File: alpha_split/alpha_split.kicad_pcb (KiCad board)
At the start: 2 copper layers, 109 x 71 mm, 135 parts, among them J1 USB_OTG, J2 USB_OTG, J3 PDI, J4 D4, J5 D5, J6 A6, J7 A7, J8 B0, J9 E2, K00 K00, K01 K01, K02 K02, K03 K03, K04 K04, K05 K05, K10 K10, K11 K11, K12 K12, K13 K13, K14 K14, K15 K15, K20 K20, K21 K21, K22 K22, K23 K23, K24 K24, K25 K25, K30 K30, K31 K31, K32 K32, K33 K33, K34 K34, K35 K35, SW1 Switch-6P-2S2T, SW2 RST_SW, U1 MCP73831, U2 MCP1700 (3.0V), U3 MCP1700 (3.3V), U4 ATXMEGA-A4U-EPAD, U5 74LVC1G34, U6 nRF24L01_module, U7 FSUSB42, U8 FSUSB42, U9 FSUSB42

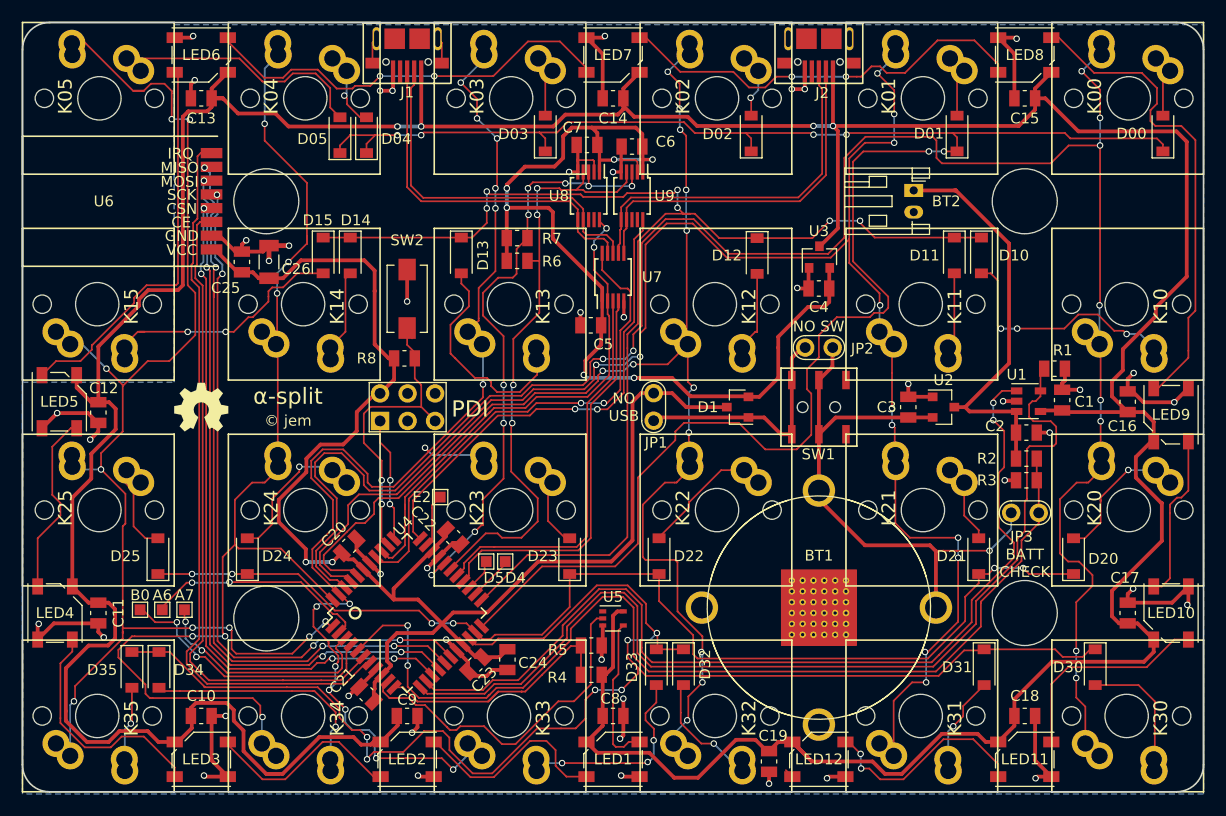
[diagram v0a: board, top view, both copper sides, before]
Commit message: minor PCB fixes and BOM updates
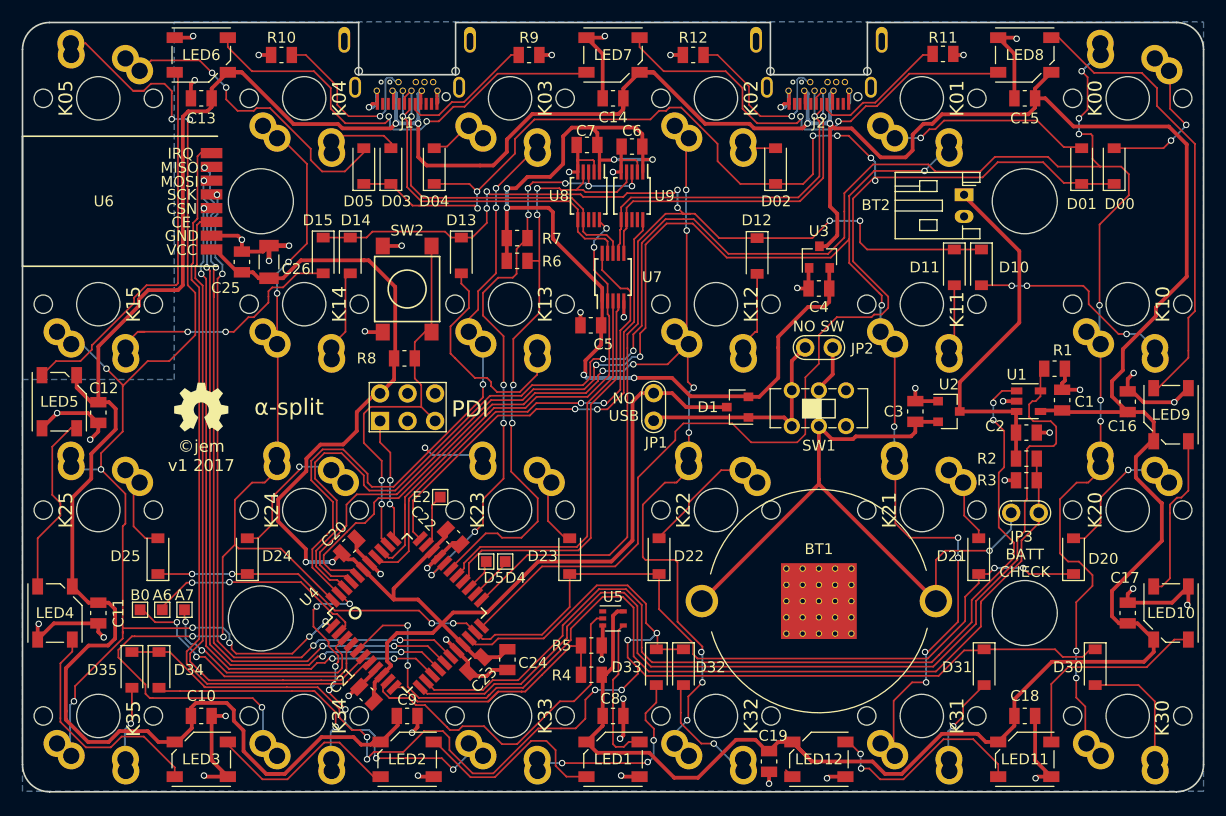
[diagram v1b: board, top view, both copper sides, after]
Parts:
- removed the BT1 at (73.5, 54.0) (x2)
- removed the REF** at (73.5, 56.0)
- removed the REF** at (75.5, 56.0)
- removed the REF** at (75.5, 54.0)
- removed the REF** at (75.5, 52.0)
- removed the REF** at (71.5, 54.0)
- removed the REF** at (73.5, 52.0)
- removed the REF** at (73.5, 54.0)
- removed the REF** at (71.5, 52.0)
- added BT1: Battery, battery:CR2032_BK-913, F.Cu at (73.5, 53.4)
- added R10: 5.1k, Resistor_SMD:R_0805_2012Metric, F.Cu at (23.9, 3.00)
- added R11: 5.1k, Resistor_SMD:R_0805_2012Metric, F.Cu at (85.0, 2.90)
- added R12: 5.1k, Resistor_SMD:R_0805_2012Metric, F.Cu at (61.9, 3.00)
- added R9: 5.1k, Resistor_SMD:R_0805_2012Metric, F.Cu at (46.8, 3.00)
- added REF**: StitchVia_0.3mm, StitchVia_2x2_0.3mm, F.Cu at (76.5, 56.4)
- added REF**: StitchVia_0.3mm, StitchVia_2x2_0.3mm, F.Cu at (70.5, 54.9)
- added REF**: StitchVia_0.3mm, StitchVia_2x2_0.3mm, F.Cu at (76.5, 53.4)
- added REF**: StitchVia_0.3mm, StitchVia_2x2_0.3mm, F.Cu at (75.0, 53.4)
- added REF**: StitchVia_0.3mm, StitchVia_2x2_0.3mm, F.Cu at (73.5, 53.4)
- added REF**: StitchVia_0.3mm, StitchVia_2x2_0.3mm, F.Cu at (72.0, 53.4)
- added REF**: StitchVia_0.3mm, StitchVia_2x2_0.3mm, F.Cu at (70.5, 53.4)
- added REF**: StitchVia_0.3mm, StitchVia_2x2_0.3mm, F.Cu at (76.5, 51.9)
- added REF**: StitchVia_0.3mm, StitchVia_2x2_0.3mm, F.Cu at (75.0, 51.9)
- added REF**: StitchVia_0.3mm, StitchVia_2x2_0.3mm, F.Cu at (73.5, 51.9)
- added REF**: StitchVia_0.3mm, StitchVia_2x2_0.3mm, F.Cu at (72.0, 51.9)
- added REF**: StitchVia_0.3mm, StitchVia_2x2_0.3mm, F.Cu at (75.0, 56.4)
- added REF**: StitchVia_0.3mm, StitchVia_2x2_0.3mm, F.Cu at (70.5, 51.9)
- added REF**: StitchVia_0.3mm, StitchVia_2x2_0.3mm, F.Cu at (76.5, 50.4)
- added REF**: StitchVia_0.3mm, StitchVia_2x2_0.3mm, F.Cu at (75.0, 50.4)
- added REF**: StitchVia_0.3mm, StitchVia_2x2_0.3mm, F.Cu at (73.5, 50.4)
- added REF**: StitchVia_0.3mm, StitchVia_2x2_0.3mm, F.Cu at (72.0, 50.4)
- added REF**: StitchVia_0.3mm, StitchVia_2x2_0.3mm, F.Cu at (73.5, 56.4)
- added REF**: StitchVia_0.3mm, StitchVia_2x2_0.3mm, F.Cu at (72.0, 56.4)
- added REF**: StitchVia_0.3mm, StitchVia_2x2_0.3mm, F.Cu at (70.5, 56.4)
- added REF**: StitchVia_0.3mm, StitchVia_2x2_0.3mm, F.Cu at (76.5, 54.9)
- added REF**: StitchVia_0.3mm, StitchVia_2x2_0.3mm, F.Cu at (75.0, 54.9)
- added REF**: StitchVia_0.3mm, StitchVia_2x2_0.3mm, F.Cu at (73.5, 54.9)
- added REF**: StitchVia_0.3mm, StitchVia_2x2_0.3mm, F.Cu at (72.0, 54.9)
- J1, J2: value USB_OTG -> USB_C_Receptacle; footprint conn_usb:USB_Micro -> conn_usb:USB_TypeC_DX07B024XJ1
- K00, K01, K02, K03, K04, K05, K10, K11, K12, K13, K14, K15, K20, K21, K22, K23, K24, K25, K30, K31, K32, K33, K34, K35: footprint switch_mx:Cherry_MX_Matias -> switch_mx:Cherry_MX_Matias_NoSilk_Back
- REF**: footprint kicad_util:StitchVia_2x2_0.3mm -> StitchVia_2x2_0.3mm
- SW1: footprint switch:Switch_Slide_SMD_6 -> switch:SlideSwitch_C&K_JS202011CQN
- SW2: footprint Button_Switch_SMD:SW_SPST_EVQPE1 -> switch:SwitchPush_C&K_PTS645_SMT
- moved D01 11.9 mm to (97.8, 13.2)
- moved D03 10.7 mm to (38.0, 13.2)
- moved REF** 5.69 mm to (70.5, 50.4)
- moved D00 5.41 mm to (100.8, 13.2)
- moved BT2 4.67 mm to (86.9, 15.9)
- moved D02 3.75 mm to (69.5, 13.2)
- moved D04 3.63 mm to (34.0, 13.2)
- moved D05 3.60 mm to (31.5, 13.2)
- moved J1 3.35 mm to (35.5, 6.85)
- moved J2 3.35 mm to (73.5, 6.85)
- moved D10 1.10 mm to (88.5, 22.6)
- moved D11 1.10 mm to (86.0, 22.6)
- moved SW2 0.90 mm to (35.5, 24.6)
- moved C3 0.76 mm to (82.4, 35.9)
- moved U2 0.64 mm to (85.5, 35.9)
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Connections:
- K02 pad 1: Net-(D02-Pad2) -> /COL2
- K02 pad 2: /COL2 -> Net-(D02-Pad2)
- K04 pad 1: Net-(D04-Pad2) -> /COL4
- K04 pad 2: /COL4 -> Net-(D04-Pad2)
- SW2 pad 1: /RST -> GND
- U7 pad 6: /D-_R -> /USB_R_D-
- U7 pad 7: /D+_R -> /USB_R_D+
- U7 pad 8: /D-_L -> /USB_L_D-
- U7 pad 9: /D+_L -> /USB_L_D+
- U8 pad 6: /D+_L -> /USB_L_D+
- U8 pad 7: /D-_L -> /USB_L_D-
- U9 pad 6: /D+_R -> /USB_R_D+
- U9 pad 7: /D-_R -> /USB_R_D-
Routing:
- net /D-_L: track 33.9 -> 0.00 mm
- net /D+_R: track 33.8 -> 0.00 mm
- net /D-_R: track 33.5 -> 0.00 mm
- net /D+_L: track 33.5 -> 0.00 mm
- net /USB_R_D+: track 0.00 -> 33.5 mm, vias 0 -> 1
- net /USB_L_D-: track 0.00 -> 33.4 mm, vias 0 -> 1
- net /USB_L_D+: track 0.00 -> 33.4 mm, vias 0 -> 1
- net /USB_R_D-: track 0.00 -> 33.1 mm, vias 0 -> 1
- net +5V: track 398.9 -> 419.1 mm
- net /BATT_IN: track 54.8 -> 72.6 mm
- net Net-(J2-PadB5): track 0.00 -> 16.5 mm, vias 0 -> 1
- net Net-(J1-PadB5): track 0.00 -> 16.5 mm, vias 0 -> 1
- net Net-(J2-PadA5): track 0.00 -> 12.6 mm
- net Net-(J1-PadA5): track 0.00 -> 12.6 mm
- net Net-(D01-Pad2): track 8.16 -> 20.6 mm, vias 0 -> 1
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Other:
- outline, holes or cut-outs redrawn
- net class Escape added: clearance 0.15, trace_width 0.15, via_dia 0.6, via_drill 0.4
- rule trace_min: 0.1524 -> 0.15
- board text added: "©jem v1 2017"
- board text removed: "© jem"

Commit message: use slots in mx footprint to appease PCB fab
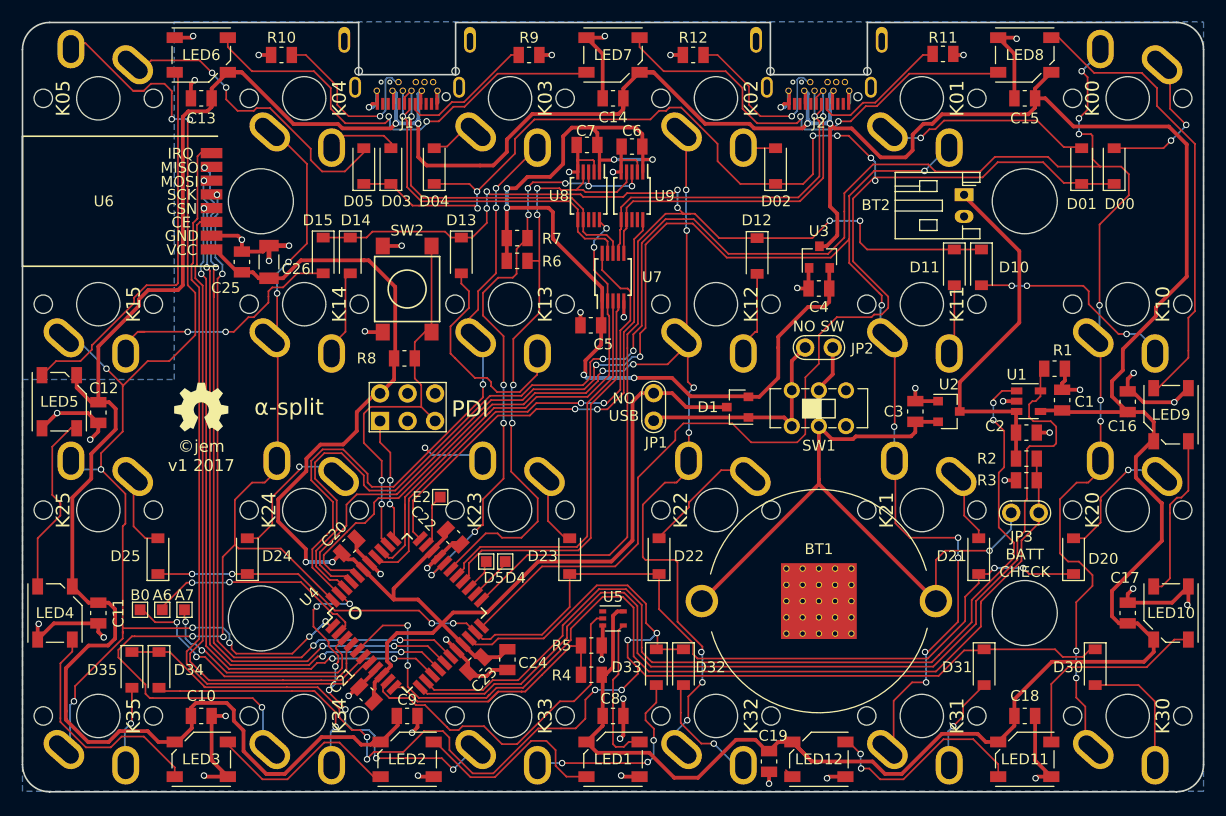
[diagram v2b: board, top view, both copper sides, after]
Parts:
- K00, K01, K02, K03, K04, K05, K10, K11, K12, K13, K14, K15, K20, K21, K22, K23, K24, K25, K30, K31, K32, K33, K34, K35: footprint switch_mx:Cherry_MX_Matias_NoSilk_Back -> switch_mx:Cherry_MX_Matias_Slots_NoSilk_Back
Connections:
- J1 pad S1: (no net) -> Net-(J1-PadS1)
- J2 pad S1: (no net) -> Net-(J2-PadS1)

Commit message: one mounting hole not aligned properly
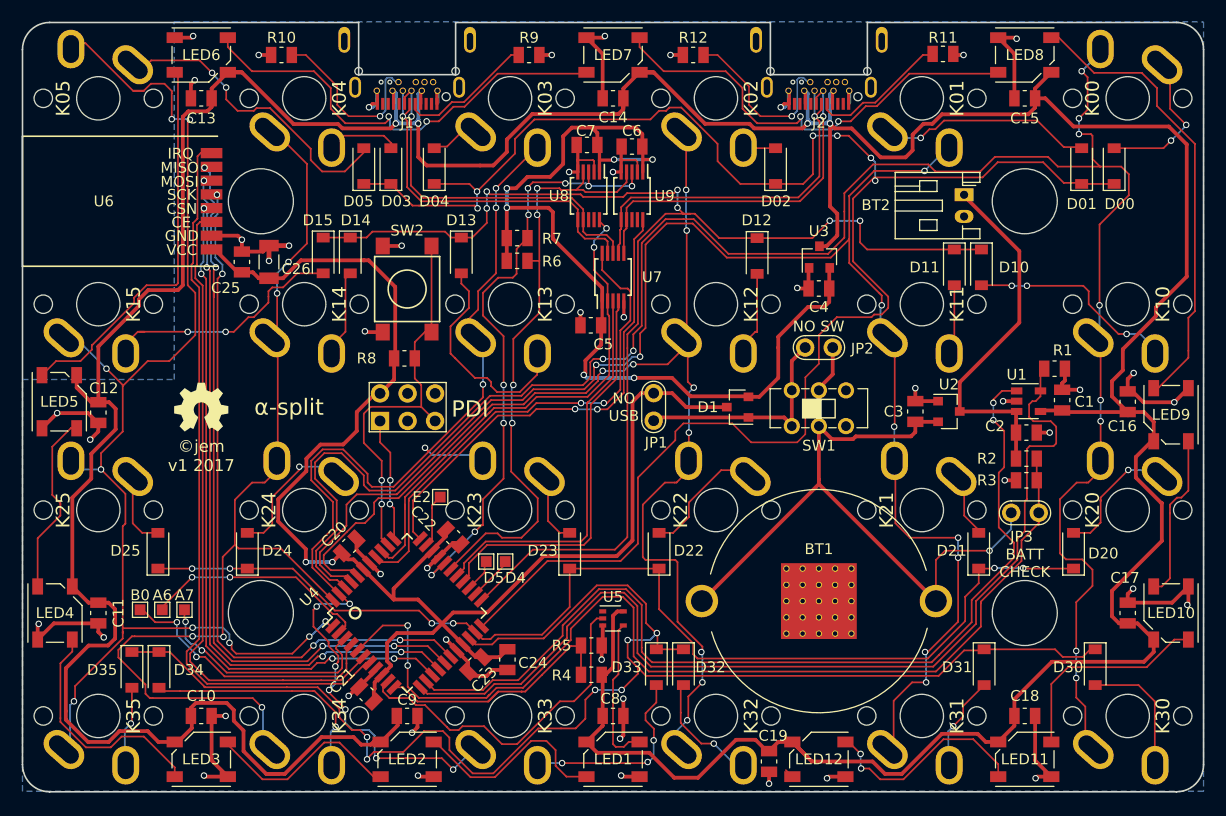
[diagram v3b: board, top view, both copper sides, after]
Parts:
- moved ? 0.50 mm to (22.0, 54.5)
- moved D20 0.50 mm to (97.0, 48.8)
- moved D21 0.50 mm to (88.2, 48.8)
- moved D22 0.50 mm to (58.8, 48.8)
- moved D23 0.50 mm to (50.5, 48.8)
- moved D24 0.50 mm to (20.8, 48.8)
- moved D25 0.50 mm to (12.5, 48.8)
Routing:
- net /ROW2: track 102.5 -> 103.8 mm
- net Net-(D25-Pad2): track 6.96 -> 8.02 mm
- net /A6: track 21.2 -> 21.8 mm
- net Net-(D21-Pad2): track 7.48 -> 6.98 mm

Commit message: reposition mounting holes
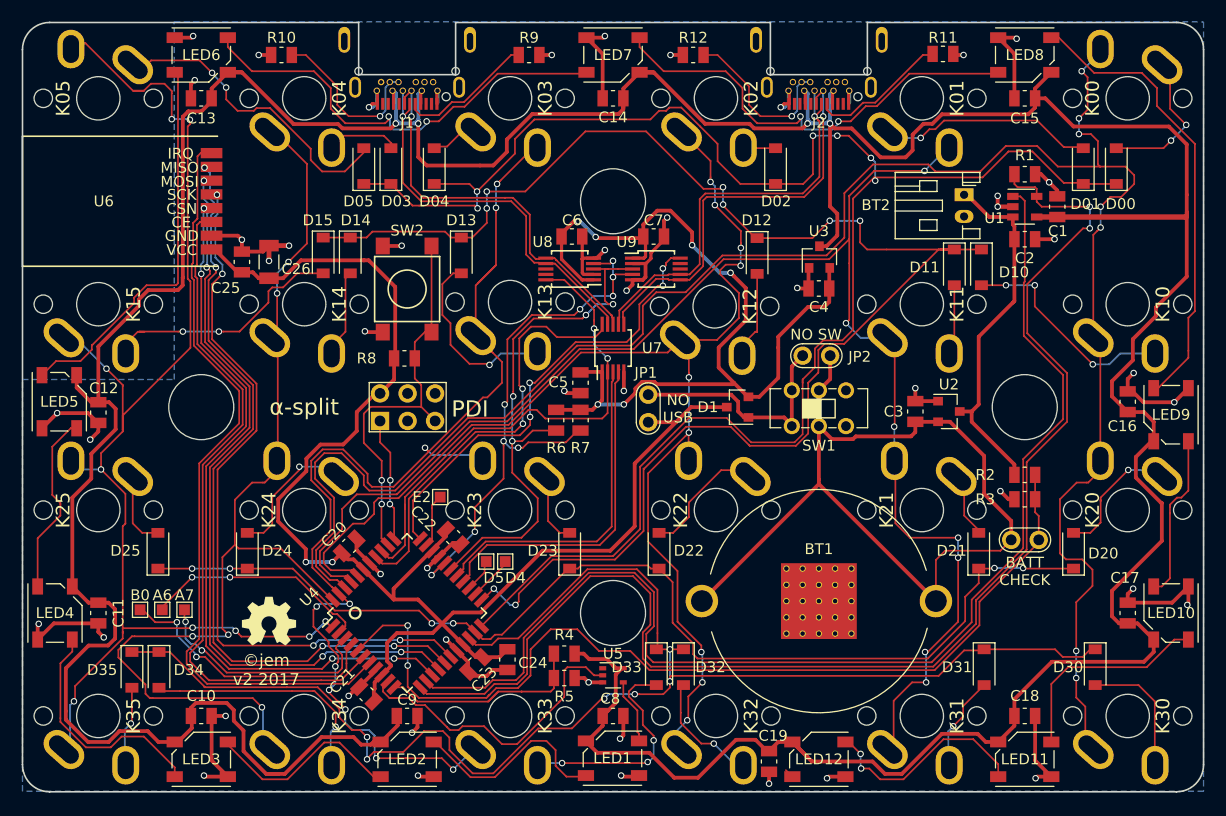
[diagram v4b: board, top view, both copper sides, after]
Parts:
- moved ? 50.0 mm to (54.5, 54.5)
- moved ? 38.0 mm to (54.5, 16.5)
- moved svg2mod 20.7 mm to (22.8, 55.2)
- moved ? 19.8 mm to (16.5, 35.5)
- moved ? 19.0 mm to (92.5, 35.5)
- moved R1 18.2 mm to (92.5, 14.0)
- moved U1 18.0 mm to (92.5, 17.0)
- moved C1 17.9 mm to (95.5, 17.0)
- moved C2 17.9 mm to (92.5, 20.0)
- moved R7 17.8 mm to (51.5, 36.7), turned to 270 degrees
- moved R6 15.1 mm to (49.2, 36.7), turned to 270 degrees
- moved C7 10.5 mm to (58.2, 19.8), turned to 0 degrees
- moved C6 9.98 mm to (50.7, 19.8), turned to 0 degrees
- moved U9 7.12 mm to (58.5, 22.8), turned to 0 degrees
- moved U8 6.97 mm to (50.5, 22.8), turned to 180 degrees
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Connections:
- J1 pad : (no net) -> Net-(J1-PadB5)
- J1 pad S1: Net-(J1-PadS1) -> (no net)
- J2 pad : (no net) -> Net-(J2-PadB5)
- J2 pad S1: Net-(J2-PadS1) -> (no net)
- U8 pad 3: /SCL -> /SDA
- U8 pad 4: /SDA -> /SCL
- U8 pad 6: /USB_L_D+ -> /USB_L_D-
- U8 pad 7: /USB_L_D- -> /USB_L_D+
- U9 pad 3: /SCL -> /SDA
- U9 pad 4: /SDA -> /SCL
- U9 pad 6: /USB_R_D+ -> /USB_R_D-
- U9 pad 7: /USB_R_D- -> /USB_R_D+
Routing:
- net /BAT_PROG: track 93.8 -> 123.8 mm, vias 0 -> 2
- net /BAT_STAT: track 87.8 -> 111.4 mm, vias 2 -> 0
- net /ROW1: track 120.6 -> 144.1 mm, vias 6 -> 8
- net /BATT_IN: track 72.6 -> 84.3 mm, vias 1 -> 0
- net Net-(LED1-Pad4): track 14.1 -> 6.00 mm
- net /USB_OE: track 46.6 -> 39.4 mm
- net /COL2: track 118.4 -> 125.6 mm
- net +3V3: track 91.7 -> 84.8 mm
- net /COL1: track 151.8 -> 145.1 mm, vias 9 -> 7
- net /SDA: track 56.0 -> 49.6 mm
- net /COL0: track 194.7 -> 188.6 mm, vias 10 -> 7
- net /D+: track 36.7 -> 30.9 mm
- net /COL3: track 107.9 -> 113.5 mm, vias 11 -> 10
- net +5V: track 419.1 -> 424.6 mm
- net /BAT_LVL: track 94.3 -> 88.9 mm
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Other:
- board text added: "©jem v2 2017"
- board text removed: "©jem v1 2017"
